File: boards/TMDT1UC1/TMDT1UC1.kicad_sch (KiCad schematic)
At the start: 40 parts, among them U1 DW3210, U2 STM32U575RGTx, U3 LIS2DH, U4 TPS61222DCK, Y1 ABM8-38.400MHZ-12-D1G-T

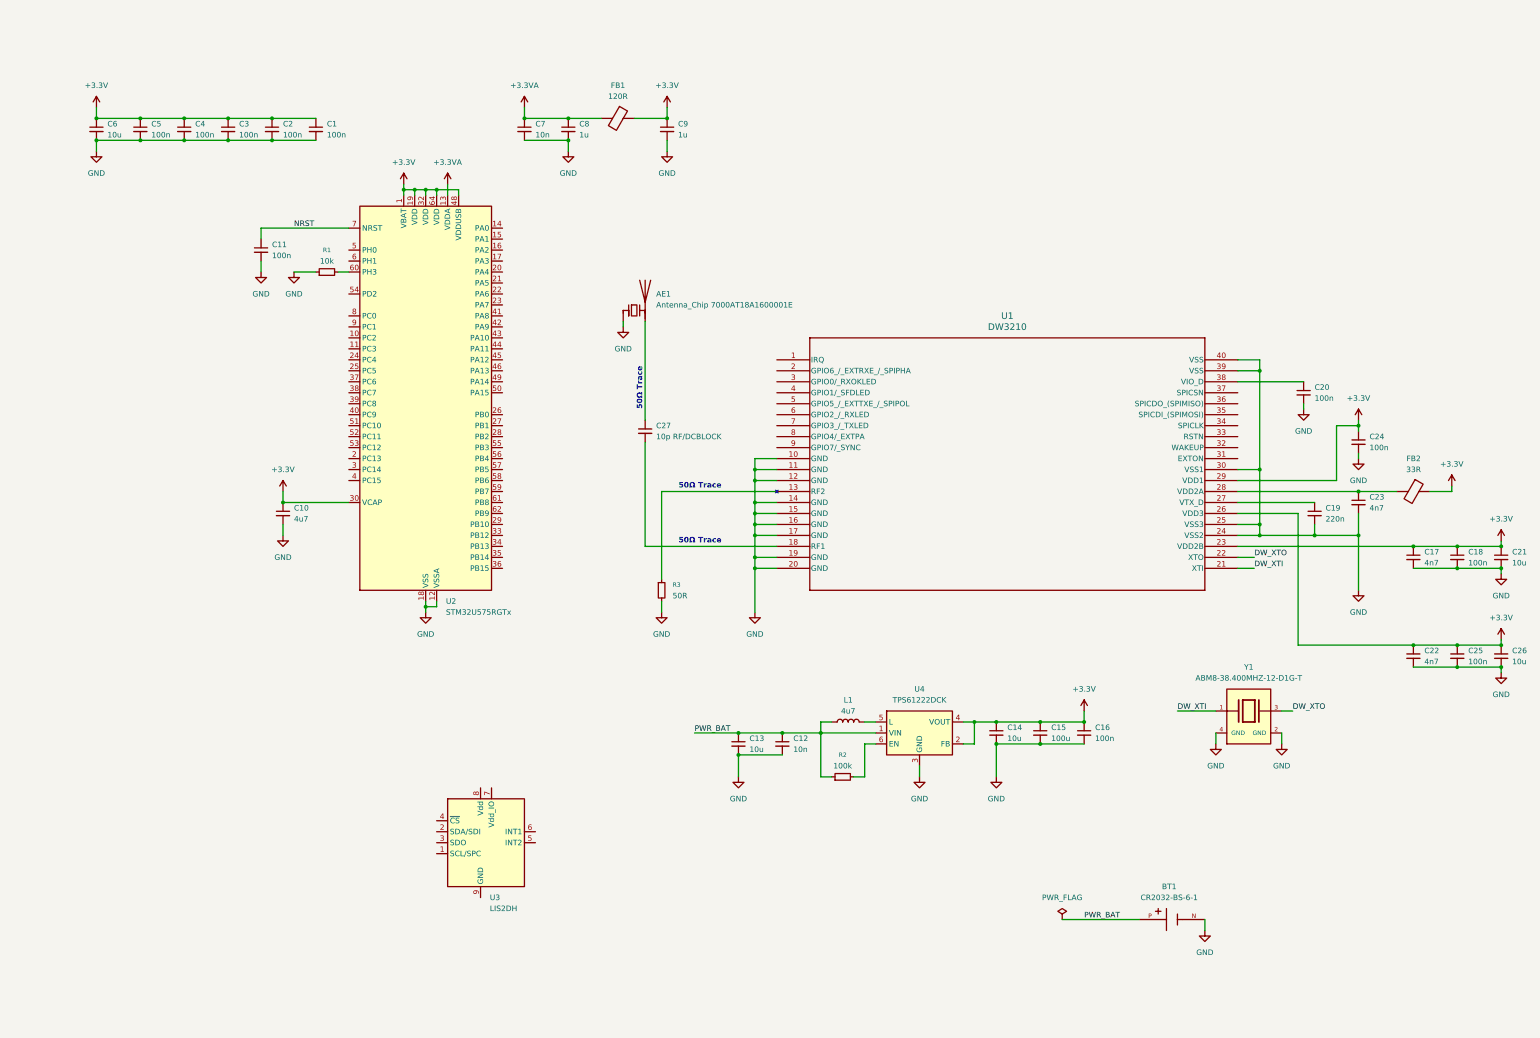
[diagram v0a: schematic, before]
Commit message: Completed base tag schematic (No PCB traces)
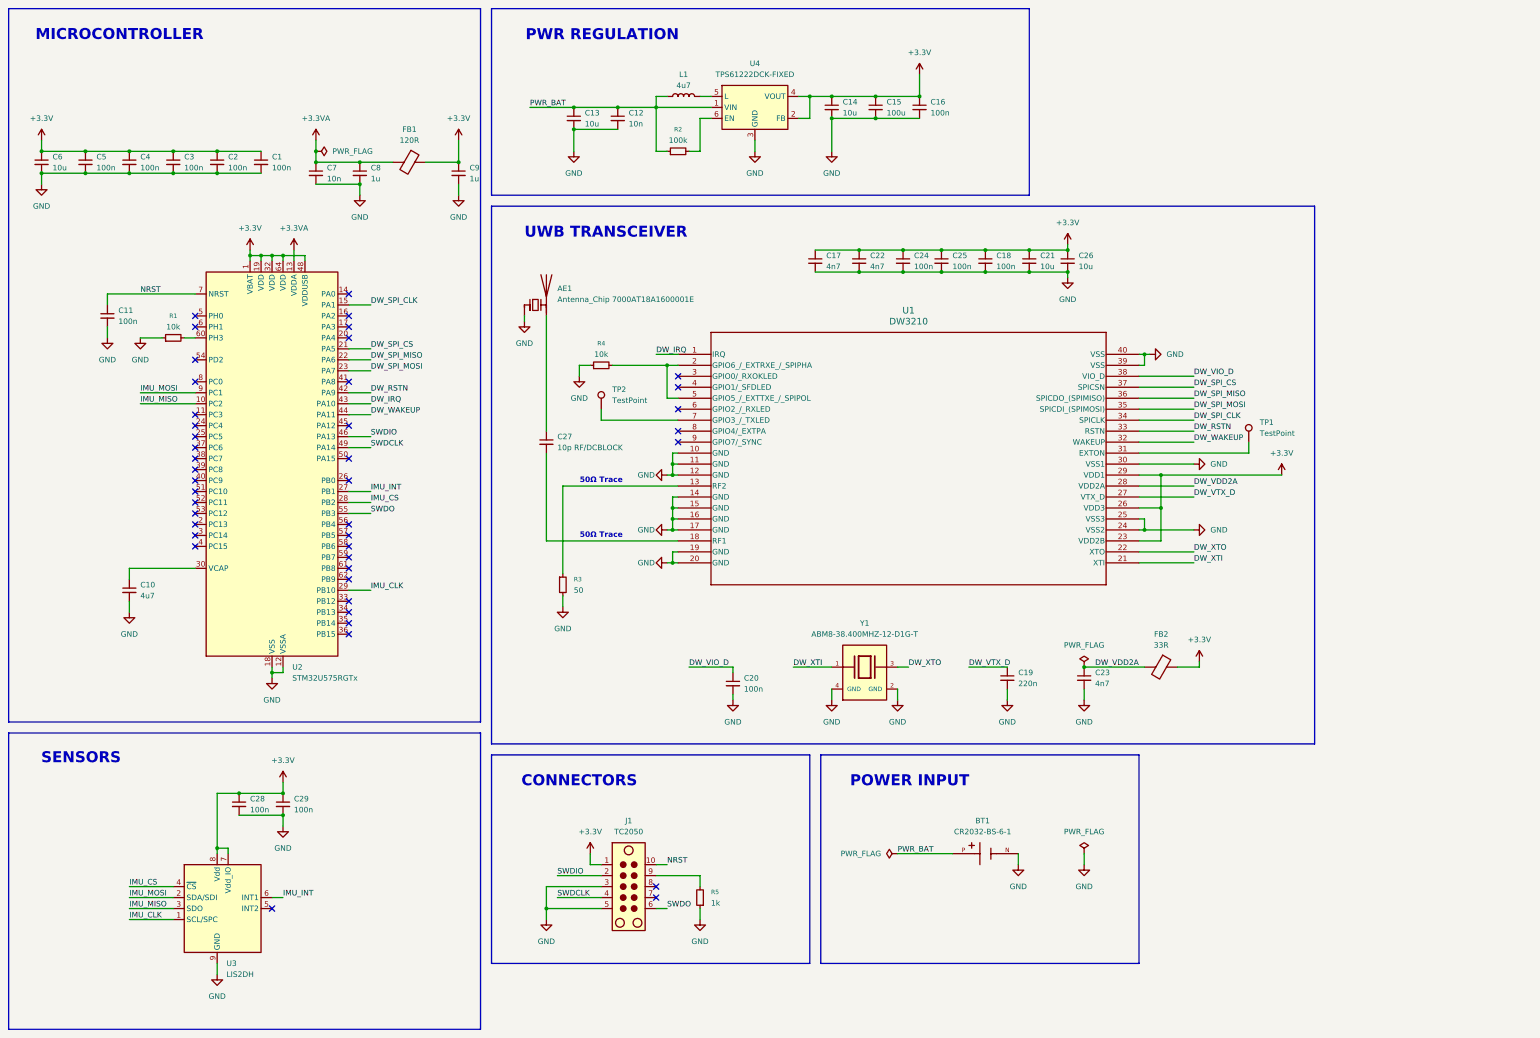
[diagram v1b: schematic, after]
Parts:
- removed U4: TPS61222DCK, Package_TO_SOT_SMD:Texas_R-PDSO-G6, symbol Regulator_Switching:TPS61222DCK
- added C28, C29: 100n, symbol Device:C_Small
- added J1: TC2050, Connector:Tag-Connect_TC2050-IDC-NL_2x05_P1.27mm_Vertical, symbol Connector:TC2050
- added R4: 10k, symbol Device:R_Small
- added R5: 1k, symbol Device:R_Small
- added TP1, TP2: TestPoint, symbol Connector:TestPoint
- added U4: TPS61222DCK-FIXED, Package_TO_SOT_SMD:Texas_R-PDSO-G6, symbol TPS61222DCK:TPS61222DCK-FIXED
- BT1: footprint BAT_CR2032-BS-6-1:BAT_CR2032-BS-6-1 -> meridian:BAT_CR2032-BS-6-1
- R3: value 50R -> 50
- U1: footprint dw3210:qfn_DW3210_QOR -> meridian:qfn_DW3210_QOR
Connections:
- net +3.3V: now also U3.7 (Vdd_IO), U3.8 (Vdd), C28.1, C29.1, J1.1, U4.2 (FB), U4.4 (VOUT); no longer C10.1, U2.30 (VCAP)
- net GND: now also U3.10 (GND), U3.11 (GND), U3.12 (GND), U3.13 (GND), U3.14 (GND), U3.9 (GND), C28.2, C29.2, J1.3, J1.5, R4.1, R5.1, U4.3 (GND)
- net NRST: now also J1.10
- net PWR_BAT: now also U4.1 (VIN)
- net at R2.2: now also U4.6 (EN)
- net DW_VDD2A: now reaches C23.1, FB2.2, U1.28 (VDD2A)
- net at L1.2: now also U4.5 (L)
- net DW_VIO_D: now reaches C20.1, U1.38 (VIO_D)
- net IMU_MISO: now reaches U2.10 (PC2)
- net IMU_MISO: now also U3.3 (SDO)
- net DW_SPI_CLK: now reaches U2.15 (PA1)
- net DW_SPI_CLK: now also U1.34 (SPICLK)
- net DW_SPI_CS: now reaches U2.21 (PA5)
- net DW_SPI_CS: now also U1.37 (SPICSN)
- net DW_SPI_MISO: now reaches U2.22 (PA6)
- net DW_SPI_MISO: now also U1.36 (SPICDO_(SPIMISO))
- net DW_SPI_MOSI: now reaches U2.23 (PA7)
- net DW_SPI_MOSI: now also U1.35 (SPICDI_(SPIMOSI))
- net IMU_INT: now reaches U2.27 (PB1)
- net IMU_INT: now also U3.6 (INT1)
- net IMU_CS: now reaches U2.28 (PB2)
- net IMU_CS: now also U3.4 (~{CS})
- net IMU_CLK: now reaches U2.29 (PB10)
- net IMU_CLK: now also U3.1 (SCL/SPC)
- net DW_RSTN: now reaches U2.42 (PA9)
- net DW_RSTN: now also U1.33 (RSTN)
- net DW_IRQ: now reaches U2.43 (PA10)
- net DW_IRQ: now also U1.1 (IRQ)
- net DW_WAKEUP: now reaches U2.44 (PA11)
- net DW_WAKEUP: now also U1.32 (WAKEUP)
- net SWDIO: now reaches U2.46 (PA13)
- net SWDIO: now also J1.2
- net SWDCLK: now reaches U2.49 (PA14)
- net SWDCLK: now also J1.4
- net SWDO: now reaches U2.55 (PB3)
- net SWDO: now also J1.6
- net IMU_MOSI: now reaches U2.9 (PC1)
- net IMU_MOSI: now also U3.2 (SDA/SDI)
- net at U1.2 (GPIO6_/_EXTRXE_/_SPIPHA): now also U1.5 (GPIO5_/_EXTTXE_/_SPIPOL), R4.2
- net DW_VTX_D: now reaches C19.1, U1.27 (VTX_D)
- net at U1.31 (EXTON): now also TP1.1
- net at U1.7 (GPIO3_/_TXLED): now also TP2.1
- new net: J1.9, R5.2
- new net: C10.1, U2.30 (VCAP)
- no-connect marks 0 -> 43
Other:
- note added: "CONNECTORS"
- note added: "MICROCONTROLLER"
- note added: "POWER INPUT"
- note added: "PWR REGULATION"
- note added: "SENSORS"
- note added: "UWB TRANSCEIVER"
- company: (none) -> GRIM
- title: (none) -> TAG_TMDT1UC1
- moved on the sheet: AE1, C1, C10, C11, C12, C13, C14, C15, C16, C17, C18, C19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

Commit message: Cleaned up visuals
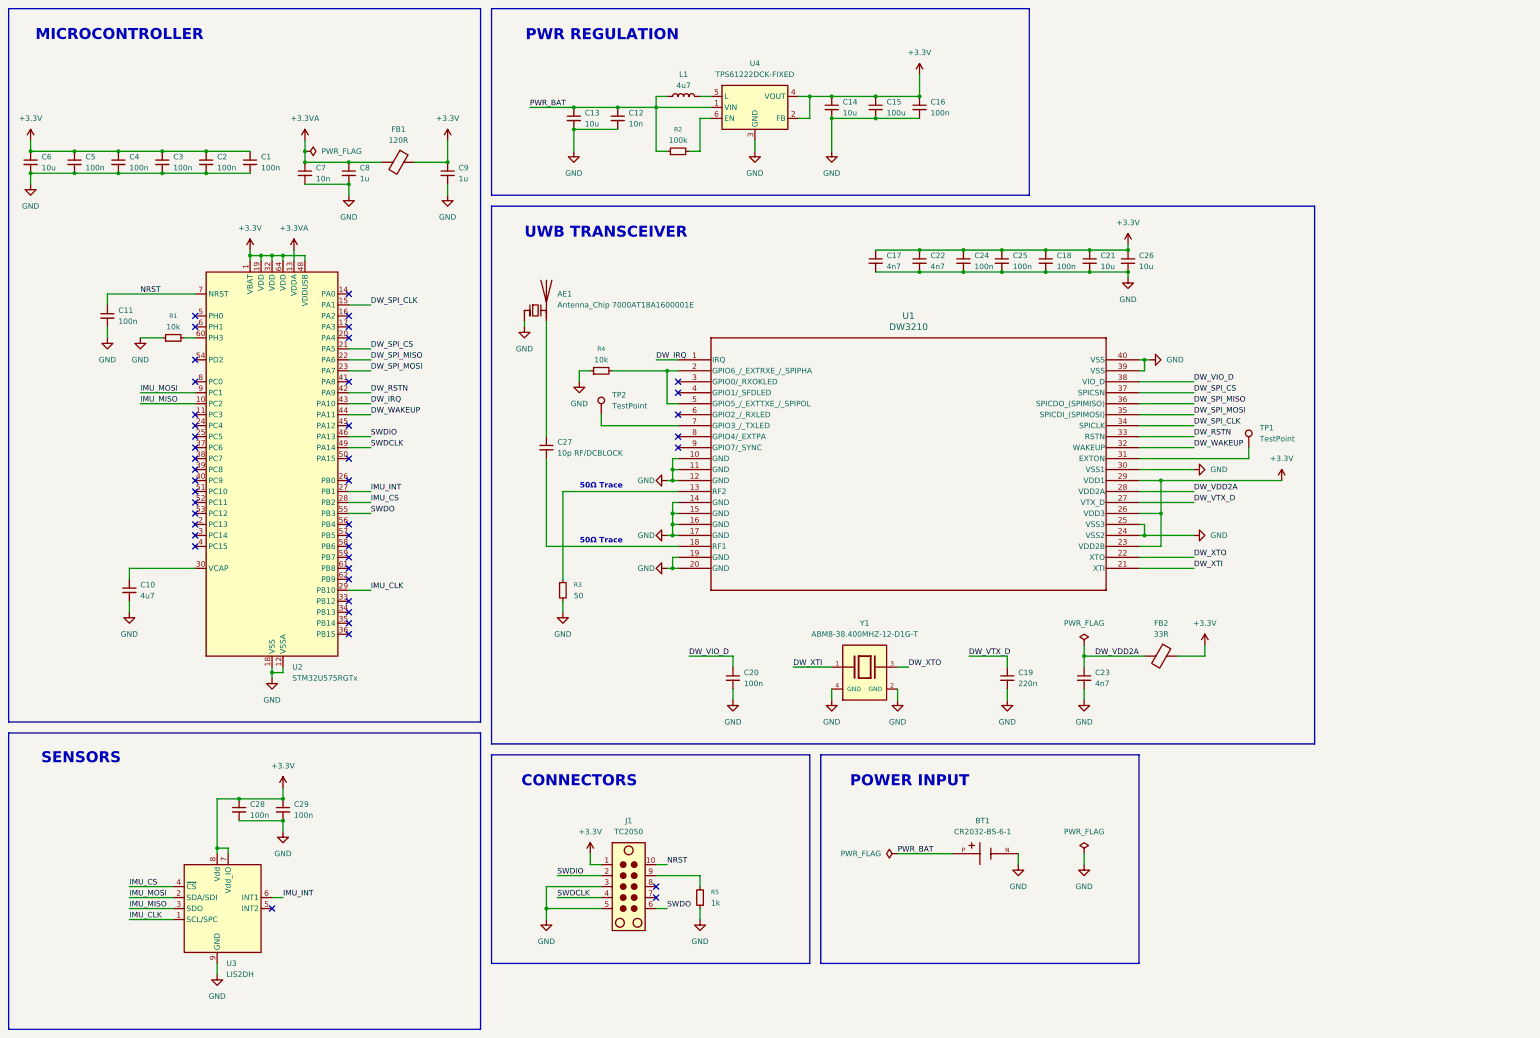
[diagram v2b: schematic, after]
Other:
- title: TAG_TMDT1UC1 -> TMDT1UC1
- moved on the sheet: AE1, C1, C17, C18, C2, C20, C21, C22, C24, C25, C26, C27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

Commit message: Started initial PCB design
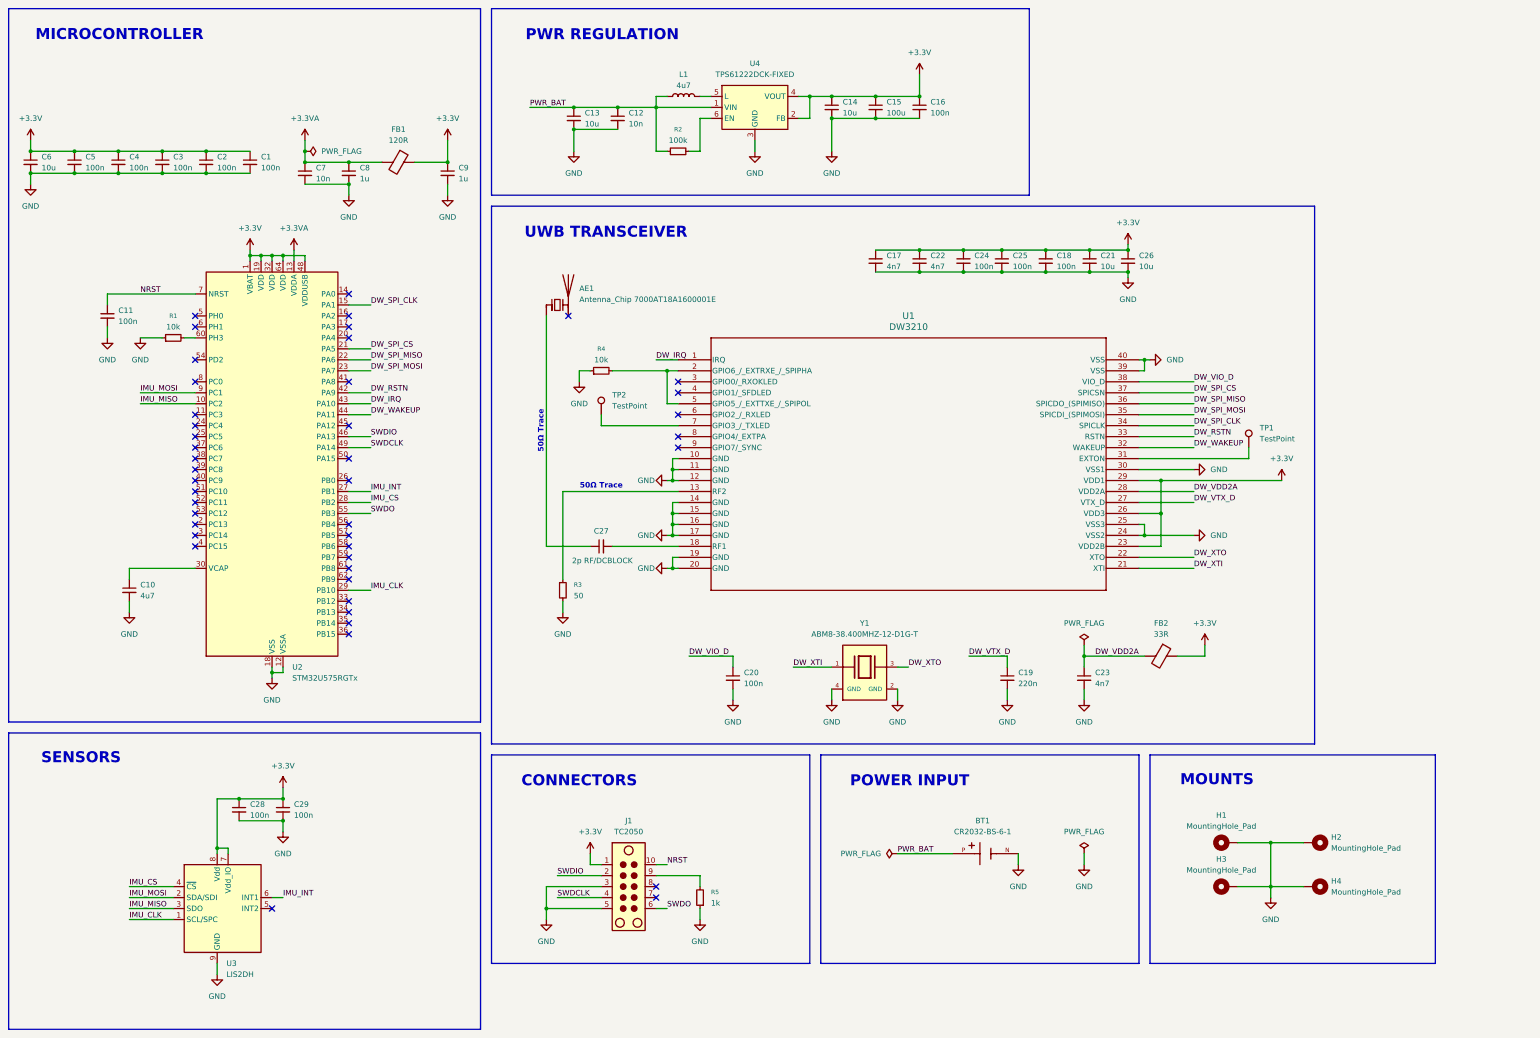
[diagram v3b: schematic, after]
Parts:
- added H1, H2, H3, H4: MountingHole_Pad, MountingHole:MountingHole_3.2mm_M3_Pad_Via, symbol Mechanical:MountingHole_Pad
- AE1: footprint (none) -> RF_Antenna:Johanson_2450AT18x100
- C1, C11, C12, C13, C14, C16, C17, C2, C20, C22, C23, C28, C29, C3, C4, C5, C6, C7: footprint (none) -> Capacitor_SMD:C_0402_1005Metric
- C10, C15, C21, C26, C8, C9: footprint (none) -> Capacitor_SMD:C_0603_1608Metric
- C18, C19, C24, C25: footprint (none) -> Capacitor_SMD:C_0201_0603Metric
- C27: value 10p RF/DCBLOCK -> 2p RF/DCBLOCK; footprint (none) -> Capacitor_SMD:C_0402_1005Metric
- FB1, FB2: footprint (none) -> Inductor_SMD:L_0603_1608Metric
- L1: footprint (none) -> Inductor_SMD:L_1210_3225Metric
- R1, R2, R3, R4, R5: footprint (none) -> Resistor_SMD:R_0402_1005Metric
- TP1, TP2: footprint (none) -> TestPoint:TestPoint_Pad_D1.0mm
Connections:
- net GND: now also H1.1, H2.1, H3.1, H4.1; no longer AE1.1 (FEED)
- net at C27.1: now also AE1.1 (FEED); no longer AE1.2 (PCB_Trace)
- no-connect marks 43 -> 44
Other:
- note added: "MOUNTS"
- moved on the sheet: AE1, C27
